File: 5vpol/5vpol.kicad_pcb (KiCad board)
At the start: 2 copper layers, 42 x 25 mm, 31 parts, among them J1 IN, J2 OUT, U1 TPS62135

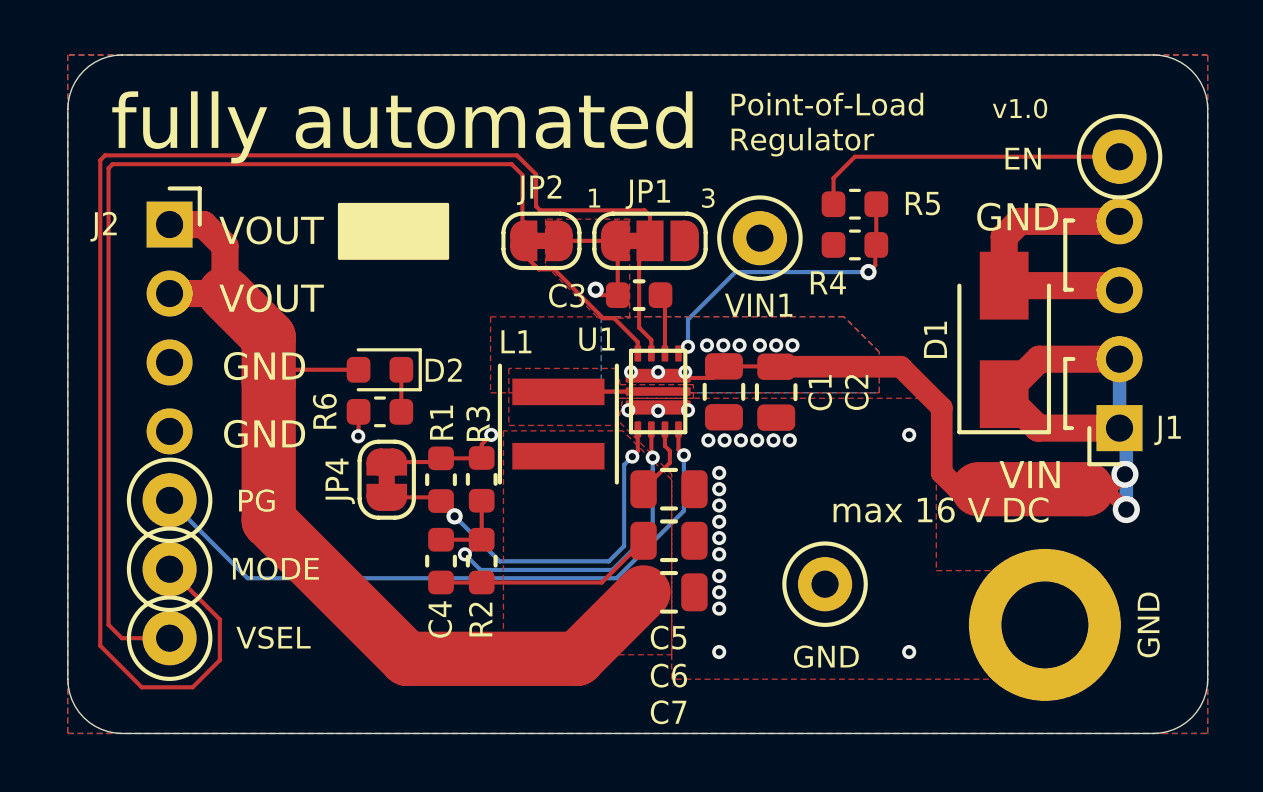
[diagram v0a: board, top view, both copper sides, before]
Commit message: update files to kicad 6
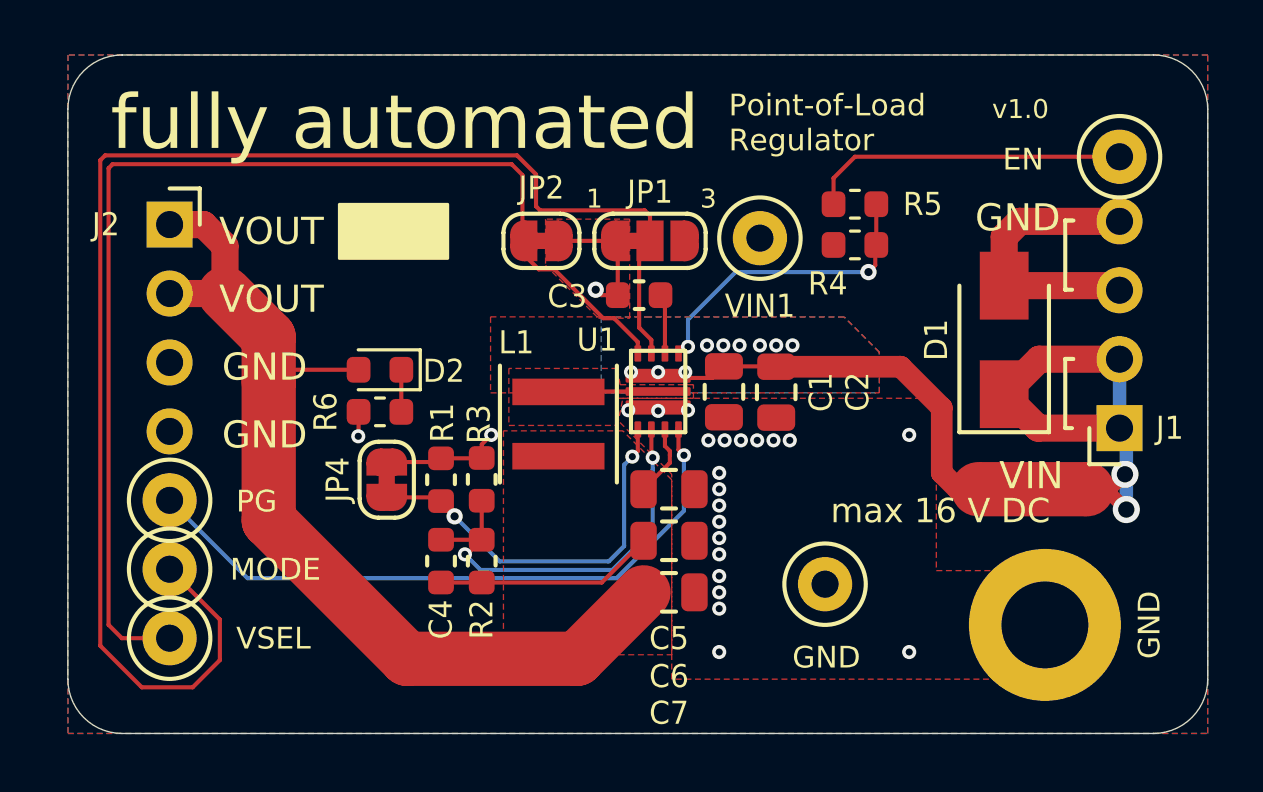
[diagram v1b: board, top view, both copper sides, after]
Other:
- net class Default removed
